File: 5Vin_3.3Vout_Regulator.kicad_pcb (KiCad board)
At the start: 2 copper layers, 11.4 x 13.5 mm, 5 parts, among them J1 PinSocket_1x04_P2.54mm_Vertic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, U1 AP2112K-3.3

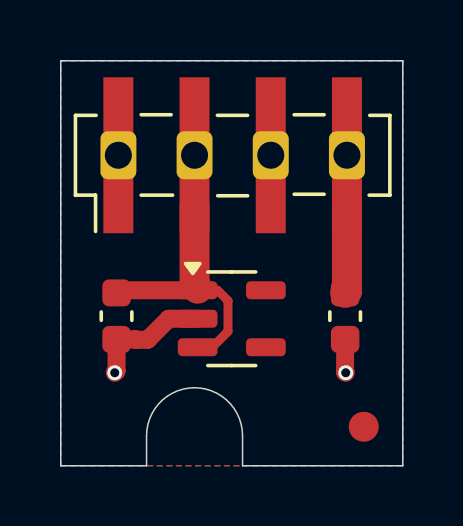
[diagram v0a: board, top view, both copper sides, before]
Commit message: Reduce the screw hole to match M2 screw
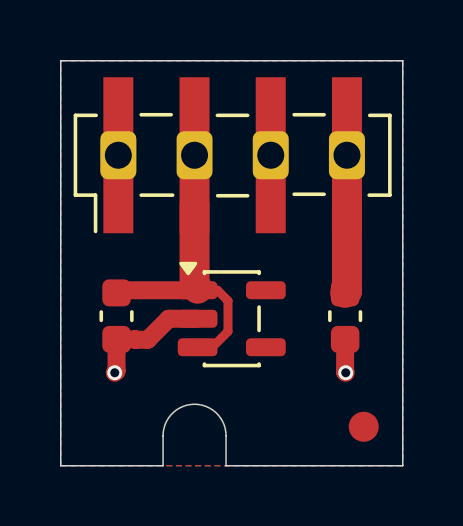
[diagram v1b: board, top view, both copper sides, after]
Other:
- outline, holes or cut-outs redrawn

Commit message: Change connector name from socket to header. Some minor traces changes.
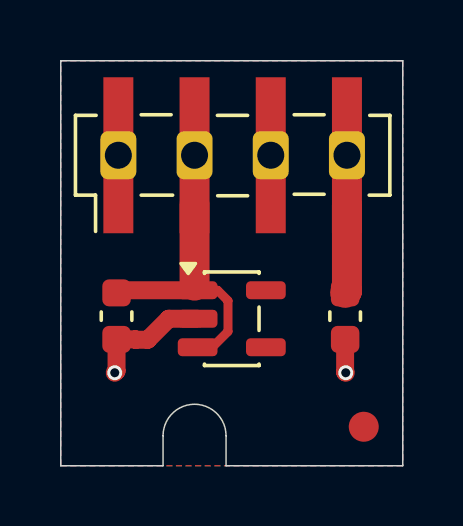
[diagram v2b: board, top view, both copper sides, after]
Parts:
- J1: value PinSocket_1x04_P2.54mm_Vertical_SMD_Pin1Left -> PinHeader_1x04_P2.54mm_Vertical_SMD_Pin1Left; footprint Library:PinSocket_1x04_P2.54mm_Vertical_SMD_Pin1Left -> PnP_Library:PinSocket_1x04_P2.54mm_Vertical_SMD_Pin1Left
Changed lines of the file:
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@@
 	(net 6 "unconnected-(J1-Pin_1-Pad1)_2")
 	(net 7 "unconnected-(U1-NC-Pad4)")
-	(footprint "Library:PinSocket_1x04_P2.54mm_Vertical_SMD_Pin1Left"
+	(footprint "PnP_Library:PinSocket_1x04_P2.54mm_Vertical_SMD_Pin1Left"
 		(layer "F.Cu")
 		(at 62.93 43.25 90)
@@
 			)
 		)
-		(property "Value" "PinSocket_1x04_P2.54mm_Vertical_SMD_Pin1Left"
+		(property "Value" "PinHeader_1x04_P2.54mm_Vertical_SMD_Pin1Left"
 			(at 0 6.68 90)
 			(layer "F.Fab")
@@
 			)
 		)
-		(property "Datasheet" ""
+		(property "Datasheet" "~"
 			(at 0 0 90)
 			(layer "F.Fab")
@@
 			)
 		)
-		(property "Description" "Regulator"
+		(property "Description" "Header"
 			(at 0 0 90)
 			(layer "F.Fab")
@@
 			)
 		)
-		(property "MFG#" ""
+		(property "MFG#" "C20071191"
 			(at 0 0 90)
 			(unlocked yes)
@@
 		)
 		(property ki_fp_filters "Connector*:*_1x??_*")
-		(sheetname "Root")
+		(sheetname "/")
 		(sheetfile "5Vin_3.3Vout_Regulator.kicad_sch")
 		(attr smd)
@@
 		)
 		(fp_text user "${REFERENCE}"
-			(at 0 0 0)
+			(at 0 0 180)
 			(layer "F.Fab")
 			(effects
@@
 			(pinfunction "Pin_1")
 			(pintype "passive+no_connect")
+			(solder_paste_margin_ratio 0.1)
 		)
 		(pad "1" thru_hole roundrect
@@
 			(remove_unused_layers no)
 			(roundrect_rratio 0.2083333333)
+			(net 5 "unconnected-(J1-Pin_1-Pad1)_1")
+			(pinfunction "Pin_1")
+			(pintype "passive+no_connect")
+		)
+		(pad "1" smd rect
+			(at 1.65 -3.81 90)
+			(size 1.9 1)
+			(layers "F.Cu" "F.Mask" "F.Paste")
 			(net 6 "unconnected-(J1-Pin_1-Pad1)_2")
 			(pinfunction "Pin_1")
 			(pintype "passive+no_connect")
-		)
-		(pad "1" smd rect
-			(at 1.65 -3.81 90)
-			(size 1.9 1)
-			(layers "F.Cu" "F.Mask" "F.Paste")
-			(net 5 "unconnected-(J1-Pin_1-Pad1)_1")
-			(pinfunction "Pin_1")
-			(pintype "passive+no_connect")
+			(solder_paste_margin_ratio 0.1)
 		)
 		(pad "2" smd rect
@@
 			(pinfunction "Pin_2")
 			(pintype "passive")
+			(solder_paste_margin_ratio 0.1)
 		)
 		(pad "2" thru_hole roundrect
@@
 			(pinfunction "Pin_2")
 			(pintype "passive")
+			(solder_paste_margin_ratio 0.1)
 		)
 		(pad "3" smd rect
@@
 			(pinfunction "Pin_3")
 			(pintype "passive")
+			(solder_paste_margin_ratio 0.1)
 		)
 		(pad "3" thru_hole roundrect
@@
 			(pinfunction "Pin_3")
 			(pintype "passive")
+			(solder_paste_margin_ratio 0.1)
 		)
 		(pad "4" smd rect
@@
 			(pinfunction "Pin_4")
 			(pintype "passive")
+			(solder_paste_margin_ratio 0.1)
 		)
 		(pad "4" thru_hole roundrect
@@
 			(pinfunction "Pin_4")
 			(pintype "passive")
+			(solder_paste_margin_ratio 0.1)
 		)
 		(embedded_fonts no)
@@
 			)
 		)
-		(property "Datasheet" ""
+		(property "Datasheet" "~"
 			(at 0 0 270)
 			(unlocked yes)
@@
 		)
 		(property ki_fp_filters "C_*")
-		(sheetname "Root")
+		(sheetname "/")
 		(sheetfile "5Vin_3.3Vout_Regulator.kicad_sch")
 		(attr smd)
@@
 		)
 		(property ki_fp_filters "SOT?23?5*")
-		(sheetname "Root")
+		(sheetname "/")
 		(sheetfile "5Vin_3.3Vout_Regulator.kicad_sch")
 		(attr smd)
@@
 			)
 		)
-		(property "Datasheet" ""
+		(property "Datasheet" "~"
 			(at 0 0 270)
 			(unlocked yes)
@@
 		)
 		(property ki_fp_filters "C_*")
-		(sheetname "Root")
+		(sheetname "/")
 		(sheetfile "5Vin_3.3Vout_Regulator.kicad_sch")
 		(attr smd)
@@
 	)
 	(segment
-		(start 61.66 47.5975)
-		(end 61.7625 47.7)
-		(width 1)
-		(layer "F.Cu")
-		(net 1)
-	)
-	(segment
